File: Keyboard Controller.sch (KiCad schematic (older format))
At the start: 1 part

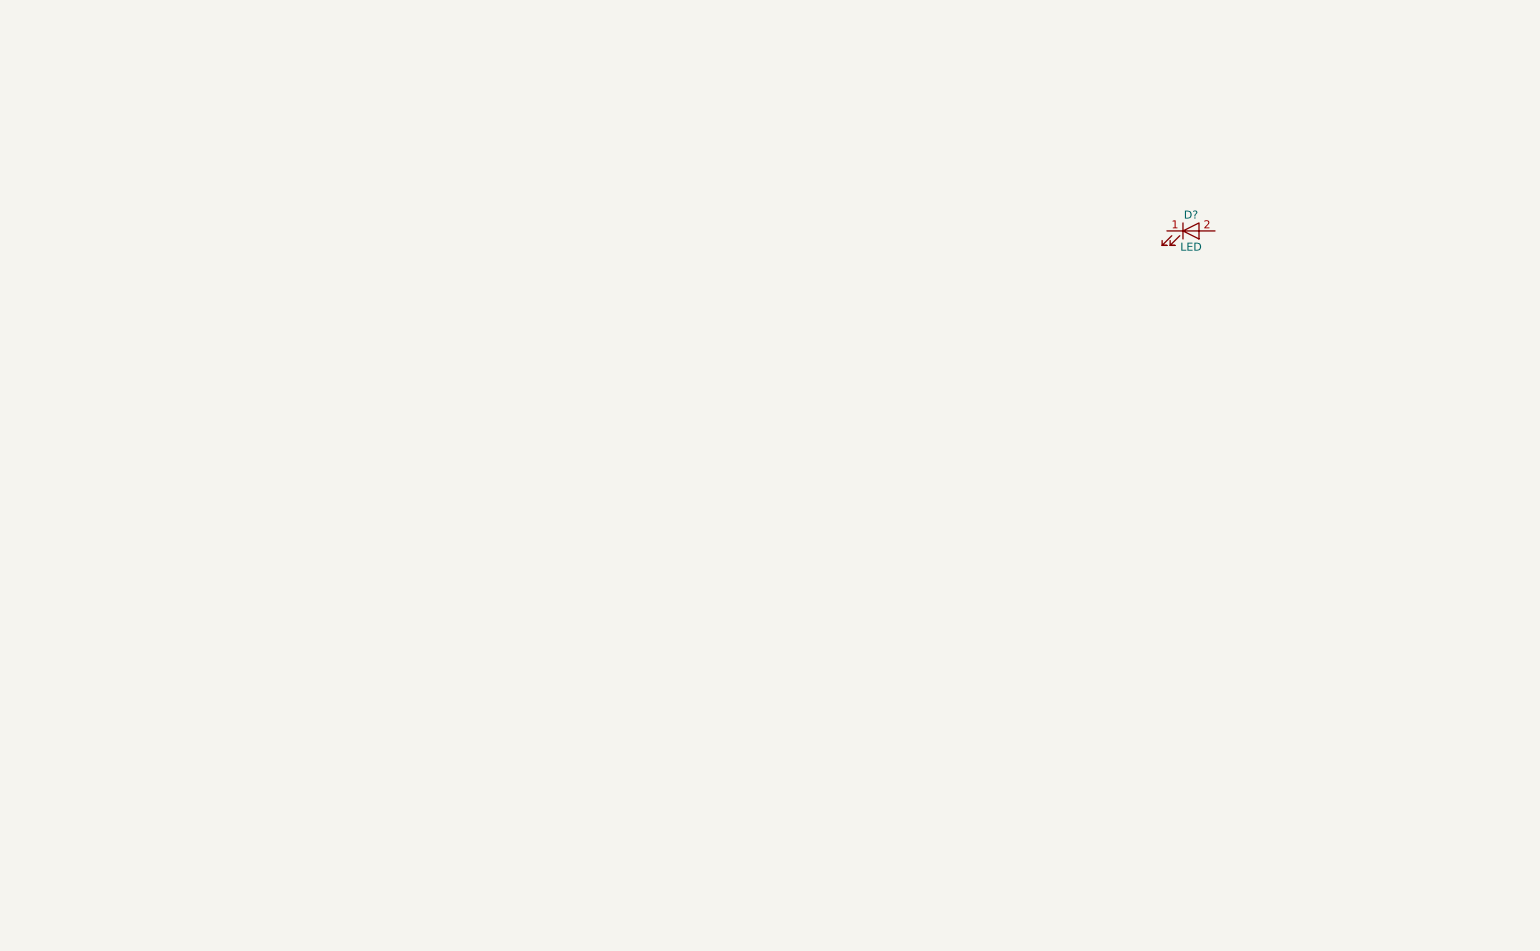
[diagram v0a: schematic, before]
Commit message: Added Teensy Library and created schematic
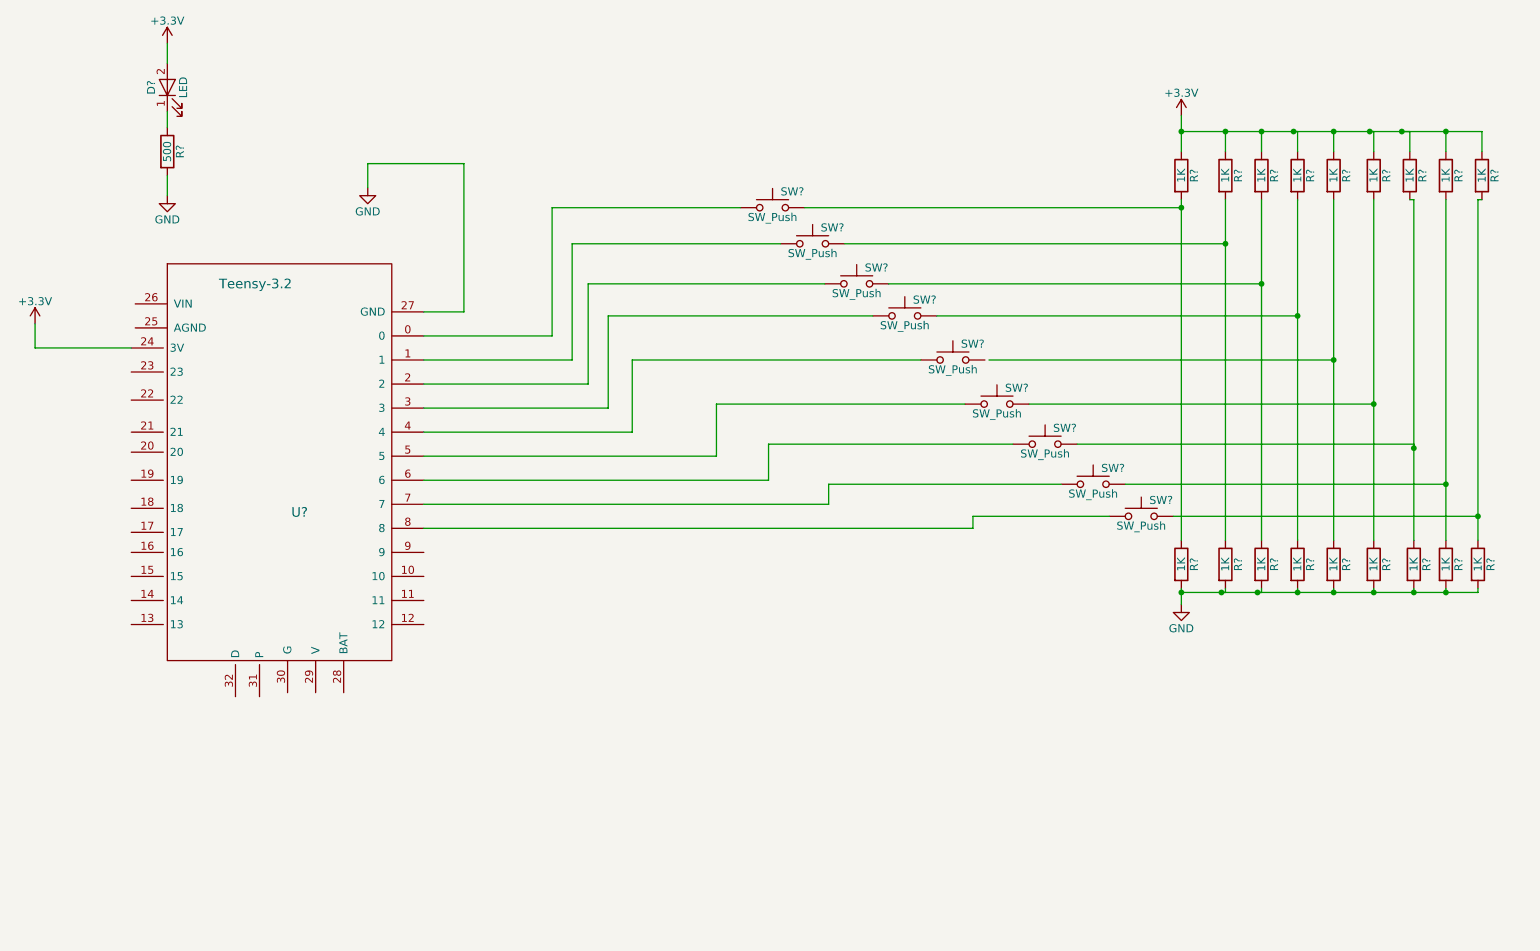
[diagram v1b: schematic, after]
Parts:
- removed D?: LED, symbol LED
- added D?: LED, symbol LED
- added R?: 500, symbol R
- added R? (x18): 1K, symbol R
- added SW? (x9): SW_Push, symbol SW_Push
- added U?: Teensy-3.2, symbol Teensy-3.2
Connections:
- new net: SW?.1, U?.0
- new net: SW?.1, U?.1
- new net: SW?.1, U?.2
- new net: SW?.1, U?.3
- new net: SW?.1, U?.4
- new net: SW?.1, U?.5
- new net: SW?.1, U?.6
- new net: SW?.1, U?.7
- new net: SW?.1, U?.8
- new net: D?.1 (K), R?.1
- new net: R?.1, R?.2, SW?.2 (x8)
- new net: R?.1, R?.2
- new net +3V3: D?.2 (A), R?.1, R?.1, R?.1, R?.1, R?.1, R?.1, R?.1, R?.1, R?.1, U?.24 (3V)
- new net GND: R?.2, R?.2, R?.2, R?.2, R?.2, R?.2, R?.2, R?.2, R?.2, R?.2, U?.27 (GND)

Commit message: Added indicator LEDs
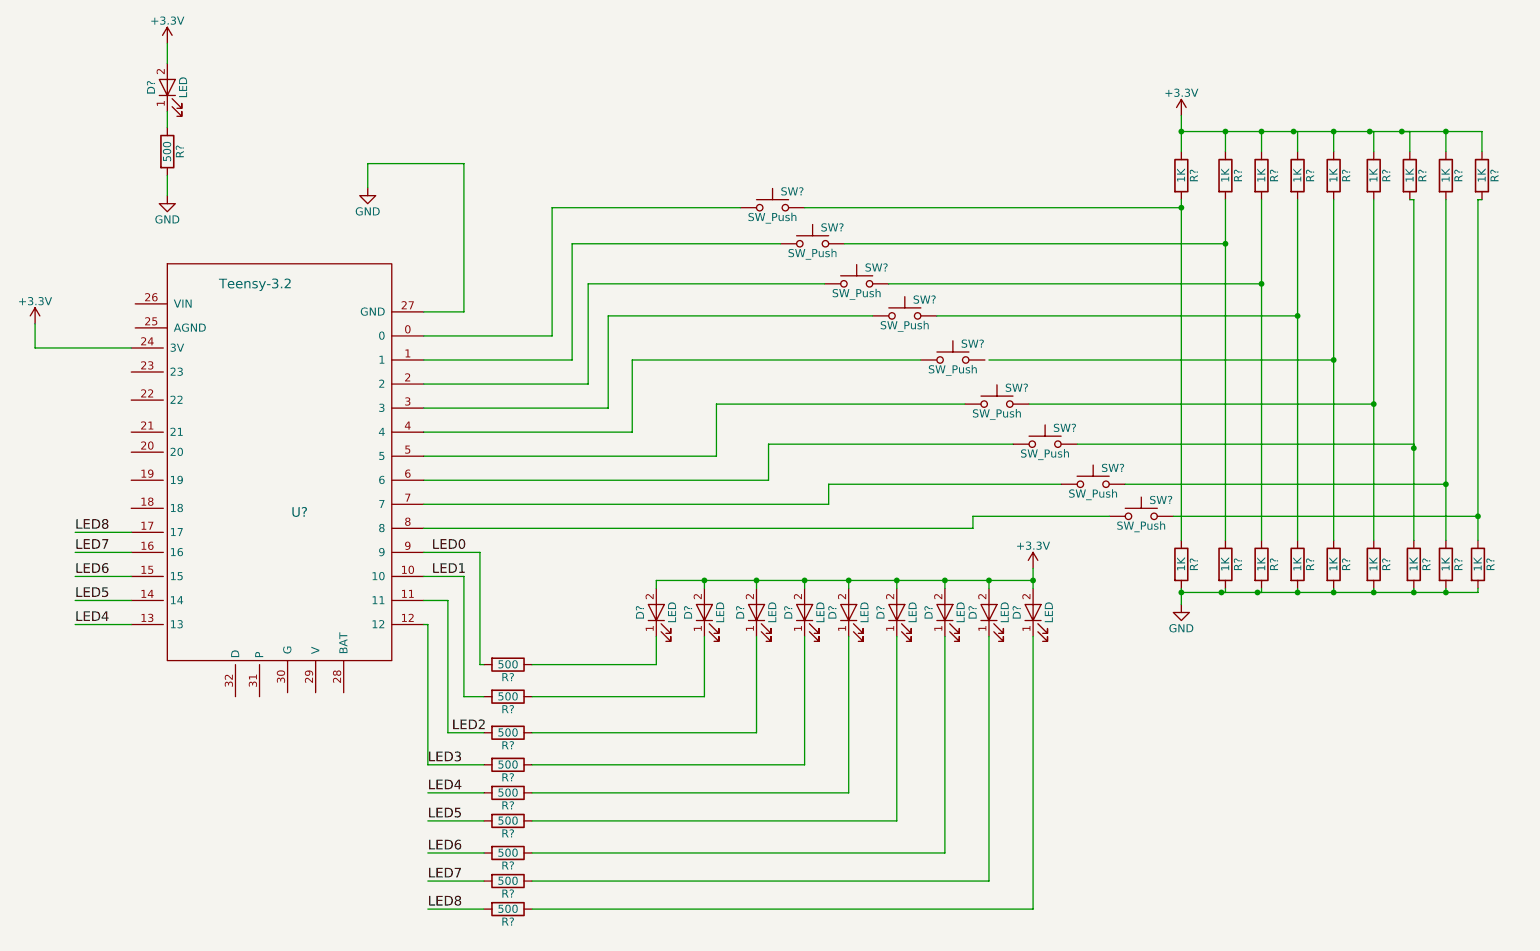
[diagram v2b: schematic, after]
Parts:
- added D? (x9): LED, symbol LED
- added R? (x9): 500, symbol R
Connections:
- net +3V3: now also D?.2 (A), D?.2 (A), D?.2 (A), D?.2 (A), D?.2 (A), D?.2 (A), D?.2 (A), D?.2 (A), D?.2 (A)
- net LED1: now reaches U?.10
- net LED1: now also R?.2
- net LED2: now reaches U?.11
- net LED2: now also R?.2
- net LED3: now reaches U?.12
- net LED3: now also R?.2
- net LED4: now reaches U?.13
- net LED4: now also R?.2
- net LED5: now reaches U?.14
- net LED5: now also R?.2
- net LED6: now reaches U?.15
- net LED6: now also R?.2
- net LED7: now reaches U?.16
- net LED7: now also R?.2
- net LED8: now reaches U?.17
- net LED8: now also R?.2
- net LED0: now reaches U?.9
- net LED0: now also R?.2
- new net: D?.1 (K), R?.1 (x9)

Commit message: Added Teensy Footprint
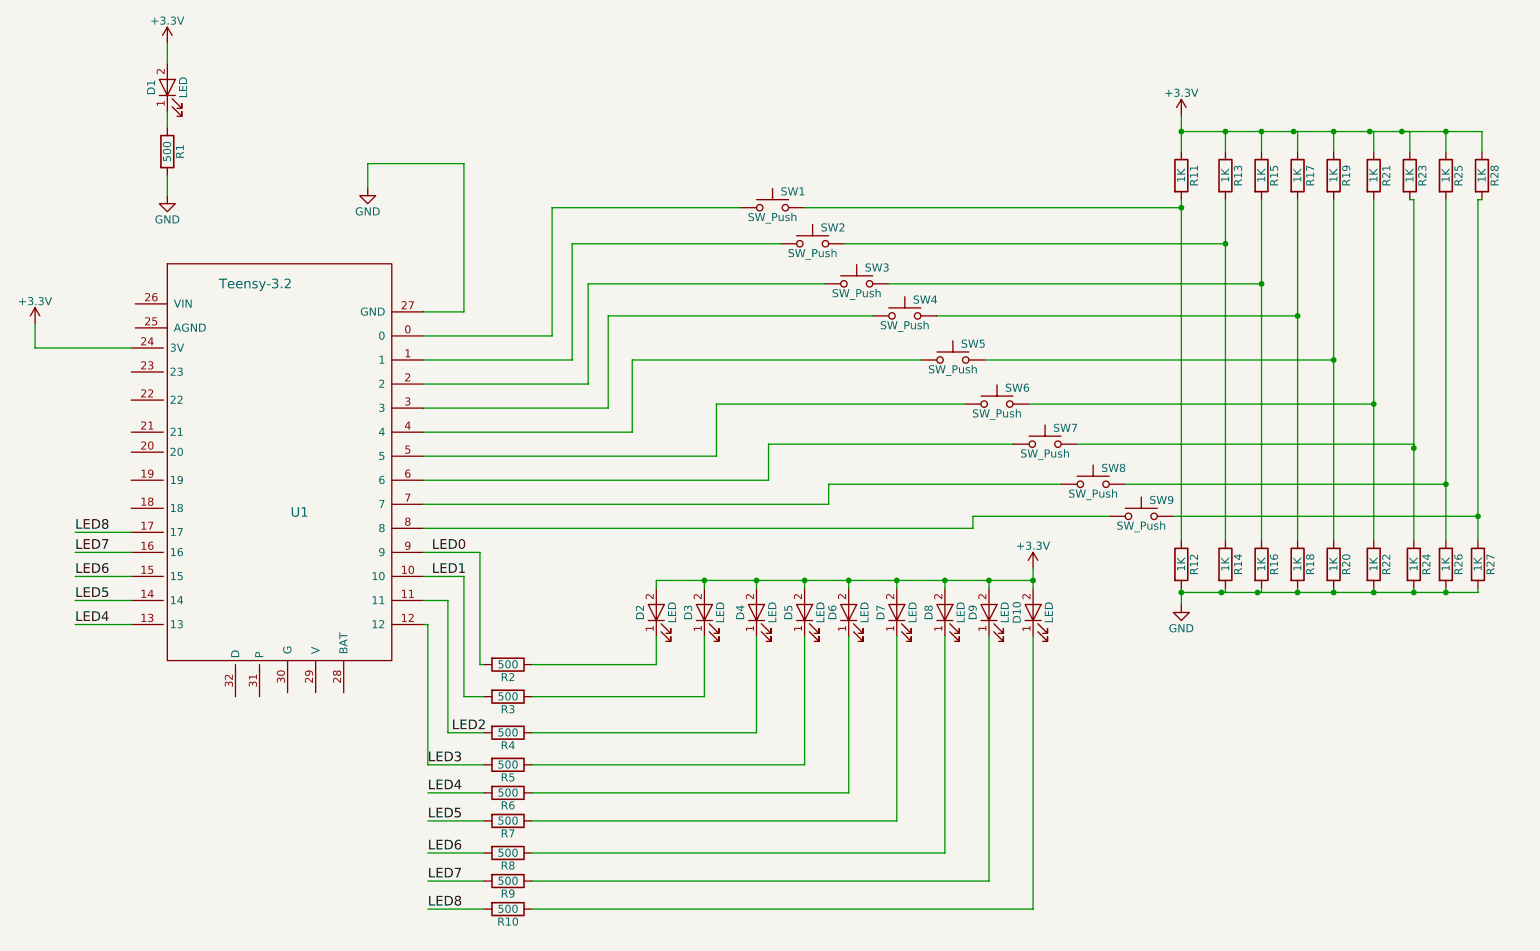
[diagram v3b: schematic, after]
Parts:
- gave numbers to parts that had none: 48
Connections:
- net at SW5.2: now also R19.2, R20.1

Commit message: Moving components before changing LED ref des index
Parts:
- D1, D10, D2, D3, D4, D5, D6, D7, D8, D9: footprint (none) -> LEDs:LED_0805
- R1, R10, R11, R12, R13, R14, R15, R16, R17, R18, R19, R2, R20, R21, R22, R23, R24, R25, R26, R27, R28, R3, R4, R5, R6, R7, R8, R9: footprint (none) -> Resistors_SMD:R_0805_HandSoldering
- SW1, SW2, SW3, SW4, SW5, SW6, SW7, SW8, SW9: footprint (none) -> Key:PTS645SK43SMTR92; MPN (none) -> PTS645SK43SMTR92
- U1: footprint (none) -> Key:Teensy-32

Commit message: Changed LED ref des indexing
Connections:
- net LED0 is gone; now on net LED1: R2.2, U1.9
- net LED1: no longer R3.2, U1.10
- net LED2: now also R3.2, U1.10; no longer R4.2, U1.11
- net LED3: now also R4.2, U1.11; no longer R5.2, U1.12
- net LED4: now also R5.2, U1.12; no longer R6.2, U1.13
- net LED5: now also R6.2, U1.13; no longer R7.2, U1.14
- net LED6: now also R7.2, U1.14; no longer R8.2, U1.15
- net LED7: now also R8.2, U1.15; no longer R9.2, U1.16
- net LED8: now also R9.2, U1.16; no longer R10.2, U1.17
- new net LED9: R10.2, U1.17
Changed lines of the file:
@@
 	3950 4575 3925 4575
 Text Label 3975 4125 0    60   ~ 0
-LED0
+LED1
 Text Label 3975 4275 0    60   ~ 0
-LED1
+LED2
 Text Label 4100 5250 0    60   ~ 0
-LED2
+LED3
 Text Label 3950 5450 0    60   ~ 0
-LED3
+LED4
 Wire Wire Line
 	4300 5625 3950 5625
@@
 	4300 6350 3950 6350
 Text Label 3950 5625 0    60   ~ 0
-LED4
+LED5
 Text Label 3950 5800 0    60   ~ 0
+LED6
+Text Label 3950 6000 0    60   ~ 0
+LED7
+Text Label 3950 6175 0    60   ~ 0
+LED8
+Text Label 3950 6350 0    60   ~ 0
+LED9
+Text Label 1750 4575 0    60   ~ 0
 LED5
-Text Label 3950 6000 0    60   ~ 0
-LED6
-Text Label 3950 6175 0    60   ~ 0
-LED7
-Text Label 3950 6350 0    60   ~ 0
-LED8
-Text Label 1750 4575 0    60   ~ 0
-LED4
 Wire Wire Line
 	1750 4575 2100 4575
@@
 	2100 4000 1750 4000
 Text Label 1750 4425 0    60   ~ 0
-LED5
+LED6
 Text Label 1750 4275 0    60   ~ 0
-LED6
+LED7
 Text Label 1750 4125 0    60   ~ 0
-LED7
+LED8
 Text Label 1750 4000 0    60   ~ 0
-LED8
+LED9
 $EndSCHEMATC

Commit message: All placements finalized
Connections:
- net SW1: now reaches SW1.1, U1.0
- net SW2: now reaches SW2.1, U1.1
- net SW3: now reaches SW3.1, U1.2
- net SW4: now reaches SW4.1, U1.3
- net SW5: now reaches SW5.1, U1.4
- net SW6: now reaches SW6.1, U1.5
- net SW7: now reaches SW7.1, U1.6
- net SW8: now reaches SW8.1, U1.7
- net SW9: now reaches SW9.1, U1.8
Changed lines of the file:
@@
 Text Label 1750 4000 0    60   ~ 0
 LED9
+Text Label 4250 2775 0    60   ~ 0
+SW1
+Text Label 4275 2925 0    60   ~ 0
+SW2
+Text Label 4275 3075 0    60   ~ 0
+SW3
+Text Label 4275 3225 0    60   ~ 0
+SW4
+Text Label 4275 3375 0    60   ~ 0
+SW5
+Text Label 4275 3525 0    60   ~ 0
+SW6
+Text Label 4275 3675 0    60   ~ 0
+SW7
+Text Label 4275 3825 0    60   ~ 0
+SW8
+Text Label 4275 3975 0    60   ~ 0
+SW9
 $EndSCHEMATC
